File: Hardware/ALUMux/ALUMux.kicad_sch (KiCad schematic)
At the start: 16 parts, among them U2MUX? 74x157

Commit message: ALUMux: Progress on routing/layout
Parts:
- added C10, C11, C12, C13, C14, C15, C16, C7, C8, C9: .1uF, Capacitor_SMD:C_1206_3216Metric_Pad1.33x1.80mm_HandSolder, symbol Device:C
- added U2MUX1, U2MUX2: 74x157, 000custom:D_R-PDSO-G16, symbol 74xx:74LS157
- added U4MUX2, U4MUX3, U4MUX4, U4MUX5, U4MUX6, U4MUX7, U4MUX8: 74x153, 000custom:D_R-PDSO-G16, symbol 74xx:74LS153
- added UADD1, UADD2: 74LS283, 000custom:D_R-PDSO-G16, symbol 74xx:74LS283
- added unit 5 of UAND1
- added UREG1: 74x377, 000custom:ON-SOIC20-WB, symbol 74xx:74LS377
- U4MUX1: renamed from U?; value 74LS153 -> 74x153; footprint (none) -> 000custom:D_R-PDSO-G16
- gave numbers to parts that had none: 12
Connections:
- net CHANGEOUT: now also J1.13 (Pin_13); no longer J3.5 (Pin_5)
- net CLK: now also J1.15 (Pin_15), UREG1.11 (CP); no longer J3.15 (Pin_15)
- net GND: now also U4MUX1.1 (Ea), C10.2, C11.2, C12.2, C13.2, C14.2, C15.2, C16.2, C7.2, C8.2, C9.2, U2MUX1.15 (E), U2MUX1.8 (GND), U2MUX2.15 (E), U2MUX2.8 (GND), U4MUX2.1 (Ea), U4MUX2.10 (I0b), U4MUX2.12 (I2b), U4MUX2.8 (GND), U4MUX3.1 (Ea), U4MUX3.10 (I0b), U4MUX3.12 (I2b), U4MUX3.8 (GND), U4MUX4.1 (Ea), U4MUX4.10 (I0b), U4MUX4.12 (I2b), U4MUX4.8 (GND), U4MUX5.1 (Ea), U4MUX5.10 (I0b), U4MUX5.12 (I2b), U4MUX5.8 (GND), U4MUX6.1 (Ea), U4MUX6.10 (I0b), U4MUX6.12 (I2b), U4MUX6.8 (GND), U4MUX7.1 (Ea), U4MUX7.10 (I0b), U4MUX7.12 (I2b), U4MUX7.8 (GND), U4MUX8.1 (Ea), U4MUX8.10 (I0b), U4MUX8.12 (I2b), U4MUX8.8 (GND), UADD1.8 (GND), UADD2.8 (GND), UAND1.7 (GND), UREG1.10 (GND), UREG1.13 (D4), UREG1.14 (D5), UREG1.17 (D6), UREG1.18 (D7), UREG1.4 (D1), UREG1.7 (D2), UREG1.8 (D3); no longer J2.9 (Pin_9), J3.3 (Pin_3)
- net IN_ACC0: now also J2.8 (Pin_8), U4MUX1.14 (S0); no longer J1.1 (Pin_1)
- net IN_ACC1: now also J2.6 (Pin_6), U4MUX2.14 (S0); no longer J1.3 (Pin_3)
- net IN_ACC2: now also J2.4 (Pin_4), U4MUX3.14 (S0); no longer J1.5 (Pin_5)
- net IN_ACC3: now also J2.2 (Pin_2), U4MUX4.14 (S0); no longer J1.7 (Pin_7)
- net IN_ACC4: now also J2.7 (Pin_7), U4MUX5.14 (S0); no longer J1.9 (Pin_9)
- net IN_ACC5: now also J2.5 (Pin_5), U4MUX6.14 (S0); no longer J1.11 (Pin_11)
- net IN_ACC6: now also J2.3 (Pin_3), U4MUX7.14 (S0); no longer J1.13 (Pin_13)
- net IN_ACC7: now also J2.1 (Pin_1), U4MUX8.14 (S0); no longer J1.15 (Pin_15)
- net IN_IMMEDIATE0: now also J1.16 (Pin_16), U2MUX1.3 (I1a); no longer J3.2 (Pin_2)
- net IN_IMMEDIATE1: now also J1.14 (Pin_14), U2MUX1.6 (I1b); no longer J3.4 (Pin_4)
- net IN_IMMEDIATE2: now also J1.12 (Pin_12), U2MUX1.10 (I1c); no longer J3.6 (Pin_6)
- net IN_IMMEDIATE3: now also J1.10 (Pin_10), U2MUX1.13 (I1d); no longer J3.8 (Pin_8)
- net IN_R0: now also J3.10 (Pin_10), U4MUX2.6 (I0a), U4MUX3.6 (I0a), U4MUX4.6 (I0a), U4MUX5.6 (I0a), U4MUX6.6 (I0a), U4MUX7.6 (I0a), U4MUX8.6 (I0a), UADD1.7 (C0); no longer J2.7 (Pin_7)
- net IN_R1: now also J3.12 (Pin_12), U4MUX2.5 (I1a), U4MUX3.5 (I1a), U4MUX4.5 (I1a), U4MUX5.5 (I1a), U4MUX6.5 (I1a), U4MUX7.5 (I1a), U4MUX8.5 (I1a); no longer J2.5 (Pin_5)
- net IN_R2: now also J3.14 (Pin_14), U4MUX2.4 (I2a), U4MUX3.4 (I2a), U4MUX4.4 (I2a), U4MUX5.4 (I2a), U4MUX6.4 (I2a), U4MUX7.4 (I2a), U4MUX8.4 (I2a); no longer J2.3 (Pin_3)
- net IN_R3: now also J3.16 (Pin_16), U4MUX2.3 (I3a), U4MUX3.3 (I3a), U4MUX4.3 (I3a), U4MUX5.3 (I3a), U4MUX6.3 (I3a), U4MUX7.3 (I3a), U4MUX8.3 (I3a); no longer J2.1 (Pin_1)
- net IN_REGDATA0: now also J1.7 (Pin_7), U2MUX1.2 (I0a); no longer J1.2 (Pin_2)
- net IN_REGDATA1: now also J1.5 (Pin_5), U2MUX1.5 (I0b); no longer J1.4 (Pin_4)
- net IN_REGDATA2: now also J1.3 (Pin_3), U2MUX1.11 (I0c); no longer J1.6 (Pin_6)
- net IN_REGDATA3: now also J1.1 (Pin_1), U2MUX1.14 (I0d); no longer J1.8 (Pin_8)
- net IN_REGDATA4: now also J1.8 (Pin_8), U2MUX2.2 (I0a); no longer J1.10 (Pin_10)
- net IN_REGDATA5: now also J1.6 (Pin_6), U2MUX2.5 (I0b); no longer J1.12 (Pin_12)
- net IN_REGDATA6: now also J1.4 (Pin_4), U2MUX2.11 (I0c); no longer J1.14 (Pin_14)
- net IN_REGDATA7: now also J1.2 (Pin_2), U2MUX2.14 (I0d); no longer J1.16 (Pin_16)
- net OUT_CARRY: now also J1.11 (Pin_11), UREG1.2 (Q0); no longer J3.11 (Pin_11)
- net OUT_RESULT0: now also J3.8 (Pin_8); no longer J2.16 (Pin_16)
- net OUT_RESULT1: now also J3.7 (Pin_7); no longer J2.14 (Pin_14)
- net OUT_RESULT2: now also J3.6 (Pin_6); no longer J2.12 (Pin_12)
- net OUT_RESULT3: now also J3.5 (Pin_5); no longer J2.10 (Pin_10)
- net OUT_RESULT4: now also J3.4 (Pin_4); no longer J2.8 (Pin_8)
- net OUT_RESULT5: now also J3.3 (Pin_3); no longer J2.6 (Pin_6)
- net OUT_RESULT6: now also J3.2 (Pin_2); no longer J2.4 (Pin_4)
- net OUT_RESULT7: now also J3.1 (Pin_1); no longer J2.2 (Pin_2)
- net OUT_RX_ID0: now also J2.16 (Pin_16); no longer J3.10 (Pin_10)
- net OUT_RX_ID1: now also J2.14 (Pin_14); no longer J3.12 (Pin_12)
- net OUT_RX_ID2: now also J2.12 (Pin_12); no longer J3.14 (Pin_14)
- net OUT_RX_ID3: now also J2.10 (Pin_10); no longer J3.16 (Pin_16)
- net SWAP_NIBBLES: now also J3.11 (Pin_11); no longer J3.9 (Pin_9)
- net VCC: now also J2.9 (Pin_9), J3.15 (Pin_15), C10.1, C11.1, C12.1, C13.1, C14.1, C15.1, C16.1, C7.1, C8.1, C9.1, U2MUX1.16 (VCC), U2MUX2.16 (VCC), U4MUX2.11 (I1b), U4MUX2.13 (I3b), U4MUX2.16 (VCC), U4MUX3.11 (I1b), U4MUX3.13 (I3b), U4MUX3.16 (VCC), U4MUX4.11 (I1b), U4MUX4.13 (I3b), U4MUX4.16 (VCC), U4MUX5.11 (I1b), U4MUX5.13 (I3b), U4MUX5.16 (VCC), U4MUX6.11 (I1b), U4MUX6.13 (I3b), U4MUX6.16 (VCC), U4MUX7.11 (I1b), U4MUX7.13 (I3b), U4MUX7.16 (VCC), U4MUX8.11 (I1b), U4MUX8.13 (I3b), U4MUX8.16 (VCC), UADD1.16 (VCC), UADD2.16 (VCC), UAND1.14 (VCC), UREG1.20 (VCC); no longer J2.13 (Pin_13), J2.15 (Pin_15), J3.1 (Pin_1)
- net ~{CARRY_WE}: now also J1.9 (Pin_9), UREG1.1 (~{E}); no longer J3.7 (Pin_7)
- net ~{IN_L}: now reaches U4MUX1.15 (Eb)
- net ~{IN_L}: now also J3.9 (Pin_9), U4MUX2.15 (Eb), U4MUX3.15 (Eb), U4MUX4.15 (Eb), U4MUX5.15 (Eb), U4MUX6.15 (Eb), U4MUX7.15 (Eb), U4MUX8.15 (Eb)
- net OPB0: now reaches U4MUX1.2 (S1)
- net OPB0: now also U2MUX1.4 (Za)
- net ADD_RIGHT0: now reaches U4MUX1.7 (Za)
- net ADD_RIGHT0: now also UADD1.6 (B1)
- net ADD_LEFT0: now reaches U4MUX1.9 (Zb)
- net ADD_LEFT0: now also UADD1.5 (A1)
- net PRESWAPPED0 renamed ADDOUT0
- net ADDOUT0: now also UADD1.4 (S1)
- net PRESWAPPED1 renamed ADDOUT1
- net ADDOUT1: now also UADD1.1 (S2)
- net PRESWAPPED2 renamed ADDOUT2
- net ADDOUT2: now also UADD1.13 (S3)
- net PRESWAPPED3 renamed ADDOUT3
- net ADDOUT3: now also UADD1.10 (S4)
- net PRESWAPPED4 renamed ADDOUT4
- net ADDOUT4: now also UADD2.4 (S1)
- net PRESWAPPED5 renamed ADDOUT5
- net ADDOUT5: now also UADD2.1 (S2)
- net PRESWAPPED6 renamed ADDOUT6
- net ADDOUT6: now also UADD2.13 (S3)
- net PRESWAPPED7 renamed ADDOUT7
- net ADDOUT7: now also UADD2.10 (S4)
- new net: UADD1.9 (C4), UADD2.7 (C0)
- new net: UADD2.9 (C4), UREG1.3 (D0)
- new net ADD_LEFT1: U4MUX2.9 (Zb), UADD1.3 (A2)
- new net ADD_LEFT2: U4MUX3.9 (Zb), UADD1.14 (A3)
- new net ADD_LEFT3: U4MUX4.9 (Zb), UADD1.12 (A4)
- new net ADD_LEFT4: U4MUX5.9 (Zb), UADD2.5 (A1)
- new net ADD_LEFT5: U4MUX6.9 (Zb), UADD2.3 (A2)
- new net ADD_LEFT6: U4MUX7.9 (Zb), UADD2.14 (A3)
- new net ADD_LEFT7: U4MUX8.9 (Zb), UADD2.12 (A4)
- new net ADD_RIGHT1: U4MUX2.7 (Za), UADD1.2 (B2)
- new net ADD_RIGHT2: U4MUX3.7 (Za), UADD1.15 (B3)
- new net ADD_RIGHT3: U4MUX4.7 (Za), UADD1.11 (B4)
- new net ADD_RIGHT4: U4MUX5.7 (Za), UADD2.6 (B1)
- new net ADD_RIGHT5: U4MUX6.7 (Za), UADD2.2 (B2)
- new net ADD_RIGHT6: U4MUX7.7 (Za), UADD2.15 (B3)
- new net ADD_RIGHT7: U4MUX8.7 (Za), UADD2.11 (B4)
- new net IMM_HIGH: J2.15 (Pin_15), U2MUX2.10 (I1c), U2MUX2.13 (I1d), U2MUX2.3 (I1a), U2MUX2.6 (I1b)
- new net OPB1: U2MUX1.7 (Zb), U4MUX2.2 (S1)
- new net OPB2: U2MUX1.9 (Zc), U4MUX3.2 (S1)
- new net OPB3: U2MUX1.12 (Zd), U4MUX4.2 (S1)
- new net OPB4: U2MUX2.4 (Za), U4MUX5.2 (S1)
- new net OPB5: U2MUX2.7 (Zb), U4MUX6.2 (S1)
- new net OPB6: U2MUX2.9 (Zc), U4MUX7.2 (S1)
- new net OPB7: U2MUX2.12 (Zd), U4MUX8.2 (S1)
- new net OPB_IS_IMM: J2.13 (Pin_13), U2MUX1.1 (S), U2MUX2.1 (S)
- no-connect marks 0 -> 7
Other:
- note added: "Find Operand B"
- note removed: "Nibbles are swapped for andi, ori, and xori"
- note removed: "TODO base off of LogiSim ALUMux. This is only a dozen chips and completely extensible, unlike the previous one at 26 chips"
- moved on the sheet: C1, C2, C3, C4, C5, C6, J1, J2, J3, U2MUX3, U2MUX4, U4MUX1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

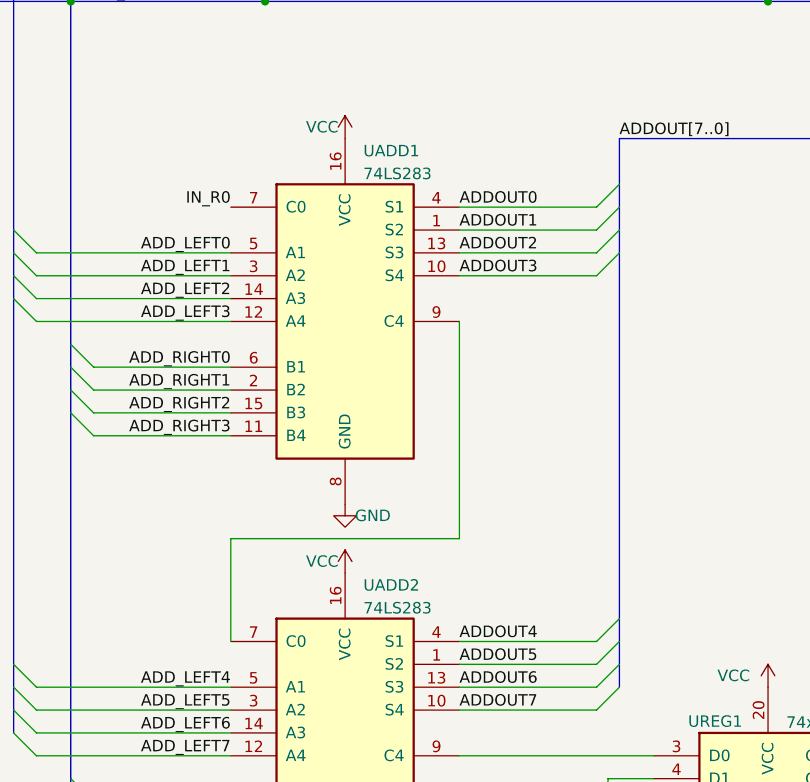
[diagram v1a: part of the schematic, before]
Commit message: Motherboard Significant Progress
This involves significant buildup of the motherboard, such as the power, oscillator, and overall design.

The motherboard schematic is in progress (some lines have yet to be connected), and the PCB layout is mostly just there to consider spacing.
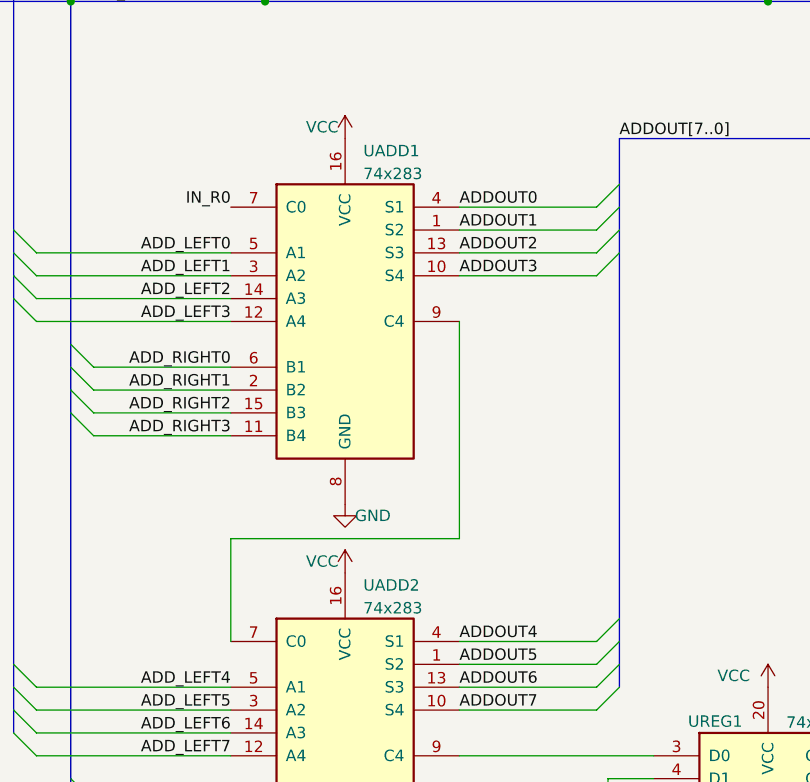
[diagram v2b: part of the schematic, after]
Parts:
- UADD1, UADD2: value 74LS283 -> 74x283
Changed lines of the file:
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@@
       (effects (font (size 1.27 1.27)) (justify left))
     )
-    (property "Value" "74LS283" (id 1) (at 206.4894 128.3771 0)
+    (property "Value" "74x283" (id 1) (at 206.4894 128.3771 0)
       (effects (font (size 1.27 1.27)) (justify left))
     )
@@
       (effects (font (size 1.27 1.27)) (justify left))
     )
-    (property "Value" "74LS283" (id 1) (at 206.4894 176.6371 0)
+    (property "Value" "74x283" (id 1) (at 206.4894 176.6371 0)
       (effects (font (size 1.27 1.27)) (justify left))
     )
@@
     )
     (path "/4ade501f-7945-4408-b9f3-a017d671fd70"
-      (reference "UADD1") (unit 1) (value "74LS283") (footprint "000custom:D_R-PDSO-G16")
+      (reference "UADD1") (unit 1) (value "74x283") (footprint "000custom:D_R-PDSO-G16")
     )
     (path "/4d46bdbd-ddf8-486c-9853-c2064c58ba4c"
-      (reference "UADD2") (unit 1) (value "74LS283") (footprint "000custom:D_R-PDSO-G16")
+      (reference "UADD2") (unit 1) (value "74x283") (footprint "000custom:D_R-PDSO-G16")
     )
     (path "/878e0ab8-92ba-4ac3-8001-5028a1e60962"
